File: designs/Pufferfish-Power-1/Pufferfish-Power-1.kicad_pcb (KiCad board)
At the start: 2 copper layers, 138 parts, among them J1 POWER_JACK_PTH, J2 POWER_JACK_PTH, J3 Molex_PicoFlex_20_Vertical, J4 Molex_MicroFit3_2x4_Receptacle, Q1 BSC028N06LS3, Q1 SiR158DP, Q2 BSC028N06LS3, Q2 SiR158DP, Q3 BSC028N06LS3, Q3 SiR158DP, Q4 BSC028N06LS3, Q4 SiR158DP, Q5 2N7002E, Q6 SiSS27DN, Q7 SiSS27DN, Q8 TP0610T, Q9 2N7002E, U1 LTC4421IUHE, U2 TPS568215RNN, U3 TPS82130

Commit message: - Changed polarity of active low LED indicators - Added footprints for test points, inductors and mounting holes - Added ESD protection on interface connectors
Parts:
- added D10: LED_SMD_0603_GREEN, LED_SMD:LED_0603_1608Metric, F.Cu at (174.5, 39.6)
- added D11: LED_SMD_0603_BLUE, LED_SMD:LED_0603_1608Metric, F.Cu at (174.5, 37.0)
- added D12: LED_SMD_0603_BLUE, LED_SMD:LED_0603_1608Metric, F.Cu at (164.5, 44.1)
- added D13: ESDLC5V0PB8, Package_DFN_QFN:UDFN-9_1.0x3.8mm_P0.5mm, F.Cu at (48.3, 61.0)
- added D14: TVS_15V_SOD123FL-2, Diode_SMD:D_SOD-123F, F.Cu at (44.0, 60.0)
- added D15: ESDLC5V0PB8, Package_DFN_QFN:UDFN-9_1.0x3.8mm_P0.5mm, F.Cu at (51.4, 61.0)
- added D3: LED_SMD_0603_YELLOW, LED_SMD:LED_0603_1608Metric, F.Cu at (168.9, 50.8)
- added D4: LED_SMD_0603_YELLOW, LED_SMD:LED_0603_1608Metric, F.Cu at (181.3, 50.8)
- added D5: LED_SMD_0603_ORANGE, LED_SMD:LED_0603_1608Metric, F.Cu at (199.1, 40.8)
- added D6: LED_SMD_0603_ORANGE, LED_SMD:LED_0603_1608Metric, F.Cu at (199.1, 32.5)
- added D7: LED_SMD_0603_RED, LED_SMD:LED_0603_1608Metric, F.Cu at (173.4, 42.2)
- added D8: LED_SMD_0603_RED, LED_SMD:LED_0603_1608Metric, F.Cu at (183.4, 32.5)
- added D9: LED_SMD_0603_GREEN, LED_SMD:LED_0603_1608Metric, F.Cu at (178.5, 37.0)
- added H1: STANDOFF_ELECTRICAL, MountingHole:MountingHole_3.2mm_M3_Pad_Via, F.Cu at (45.2, 43.7)
- added H2: STANDOFF_ELECTRICAL, MountingHole:MountingHole_3mm_Pad_Via, F.Cu at (45.0, 51.5)
- added H3: STANDOFF_ELECTRICAL, MountingHole:MountingHole_3.2mm_M3_Pad_Via, F.Cu at (53.1, 43.7)
- added H4: STANDOFF_ELECTRICAL, MountingHole:MountingHole_3mm_Pad_Via, F.Cu at (52.5, 51.5)
- added H5: STANDOFF_ELECTRICAL, MountingHole:MountingHole_3mm_Pad_Via, F.Cu at (60.9, 43.5)
- added H6: STANDOFF_ELECTRICAL, MountingHole:MountingHole_3mm_Pad_Via, F.Cu at (60.1, 51.5)
- added J5: Molex_MicroFit_2P, Connector_Molex:Molex_Micro-Fit_3.0_43045-0200_2x01_P3.00mm_Horizontal, F.Cu at (76.4, 49.7)
- added J6: Molex_MicroFit_2P, Connector_Molex:Molex_Micro-Fit_3.0_43045-0200_2x01_P3.00mm_Horizontal, F.Cu at (85.7, 49.7)
- added L1: PM2201.122NLT, Pufferfish:L_Pulse_PA5001, F.Cu at (180.3, 87.6)
- added Q10: 2N7002E, Package_TO_SOT_SMD:SOT-23, F.Cu at (164.6, 51.8)
- added Q11: 2N7002E, Package_TO_SOT_SMD:SOT-23, F.Cu at (177.0, 51.8)
- added Q12: 2N7002E, Package_TO_SOT_SMD:SOT-23, F.Cu at (194.8, 41.7)
- added Q13: 2N7002E, Package_TO_SOT_SMD:SOT-23, F.Cu at (194.8, 33.5)
- added Q14: TP0610T, Package_TO_SOT_SMD:SOT-23, F.Cu at (93.7, 68.9)
- added Q14: 2N7002E, Package_TO_SOT_SMD:SOT-23, F.Cu at (164.6, 40.6)
- added Q15: TP0610T, Package_TO_SOT_SMD:SOT-23, F.Cu at (89.2, 68.9)
- added Q15: 2N7002E, Package_TO_SOT_SMD:SOT-23, F.Cu at (170.2, 38.0)
- added Q16: TP0610T, Package_TO_SOT_SMD:SOT-23, F.Cu at (89.2, 59.8)
- added Q16: 2N7002E, Package_TO_SOT_SMD:SOT-23, F.Cu at (169.1, 42.6)
- added Q17: TP0610T, Package_TO_SOT_SMD:SOT-23, F.Cu at (93.7, 64.4)
- added Q17: 2N7002E, Package_TO_SOT_SMD:SOT-23, F.Cu at (174.6, 33.5)
- added Q18: TP0610T, Package_TO_SOT_SMD:SOT-23, F.Cu at (89.2, 64.4)
- added Q18: 2N7002E, Package_TO_SOT_SMD:SOT-23, F.Cu at (170.2, 33.5)
- added Q19: TP0610T, Package_TO_SOT_SMD:SOT-23, F.Cu at (93.7, 59.8)
- added Q19: 2N7002E, Package_TO_SOT_SMD:SOT-23, F.Cu at (179.1, 33.5)
- added R24: RES_330R_0603_SMD, Pufferfish:RES_SMD_0603, F.Cu at (168.9, 53.4)
- added R25: RES_330R_0603_SMD, Pufferfish:RES_SMD_0603, F.Cu at (181.2, 53.4)
- added R53: RES_330R_0603_SMD, Pufferfish:RES_SMD_0603, F.Cu at (199.1, 43.3)
- added R54: RES_330R_0603_SMD, Pufferfish:RES_SMD_0603, F.Cu at (199.1, 35.0)
- added R55: RES_330R_0603_SMD, Pufferfish:RES_SMD_0603, F.Cu at (177.4, 42.2)
- added R56: RES_330R_0603_SMD, Pufferfish:RES_SMD_0603, F.Cu at (182.5, 39.6)
- added R57: RES_330R_0603_SMD, Pufferfish:RES_SMD_0603, F.Cu at (187.4, 32.5)
- added R58: RES_330R_0603_SMD, Pufferfish:RES_SMD_0603, F.Cu at (178.5, 39.6)
- added R59: RES_330R_0603_SMD, Pufferfish:RES_SMD_0603, F.Cu at (182.5, 37.0)
- added R60: RES_330R_0603_SMD, Pufferfish:RES_SMD_0603, F.Cu at (173.3, 44.8)
- added TP1: TP_TH_KEYSTONE_5010, TestPoint:TestPoint_Keystone_5010-5014_Multipurpose, F.Cu at (59.5, 60.8)
- added TP10: TP_TH_KEYSTONE_5126, TestPoint:TestPoint_Keystone_5010-5014_Multipurpose, F.Cu at (79.4, 60.1)
- added TP11: TP_TH_KEYSTONE_5126, TestPoint:TestPoint_Keystone_5010-5014_Multipurpose, F.Cu at (74.4, 65.1)
- added TP12: TP_TH_KEYSTONE_5126, TestPoint:TestPoint_Keystone_5010-5014_Multipurpose, F.Cu at (74.4, 60.1)
- added TP13: TP_TH_KEYSTONE_5126, TestPoint:TestPoint_Keystone_5010-5014_Multipurpose, F.Cu at (84.5, 60.1)
- added TP14: TP_TH_KEYSTONE_5126, TestPoint:TestPoint_Keystone_5010-5014_Multipurpose, F.Cu at (84.5, 65.1)
- added TP2: TP_TH_KEYSTONE_5010, TestPoint:TestPoint_Keystone_5010-5014_Multipurpose, F.Cu at (92.8, 42.3)
- added TP3: TP_TH_KEYSTONE_5010, TestPoint:TestPoint_Keystone_5010-5014_Multipurpose, F.Cu at (92.8, 47.3)
- added TP4: TP_TH_KEYSTONE_5126, TestPoint:TestPoint_Keystone_5010-5014_Multipurpose, F.Cu at (237.0, 56.3)
- added TP5: TP_TH_KEYSTONE_5010, TestPoint:TestPoint_Keystone_5010-5014_Multipurpose, F.Cu at (249.9, 47.7)
- added TP6: TP_TH_KEYSTONE_5010, TestPoint:TestPoint_Keystone_5010-5014_Multipurpose, F.Cu at (237.0, 47.7)
- added TP7: TP_SMT_KEYSTONE_5019, Pufferfish:TP380X203, F.Cu at (165.2, 36.5)
- added TP8: TP_SMT_KEYSTONE_5019, Pufferfish:TP380X203, F.Cu at (165.2, 33.0)
- added TP9: TP_TH_KEYSTONE_5126, TestPoint:TestPoint_Keystone_5010-5014_Multipurpose, F.Cu at (79.4, 65.1)
- moved C1 25.4 mm to (115.6, 156.2)
- moved C10 25.4 mm to (183.1, 133.3)
- moved C11 25.4 mm to (187.7, 129.1)
- moved C12 25.4 mm to (161.4, 126.4)
- moved C13 25.4 mm to (176.1, 126.4)
- moved C14 25.4 mm to (96.5, 116.8)
- moved C15 25.4 mm to (92.1, 116.8)
- moved C16 25.4 mm to (91.4, 119.3)
- moved C17 25.4 mm to (113.2, 108.4)
- moved C18 25.4 mm to (110.3, 108.4)
- moved C19 25.4 mm to (111.9, 105.9)
- moved C2 25.4 mm to (115.6, 158.7)
- moved C20 25.4 mm to (107.5, 105.9)
- moved C21 25.4 mm to (103.1, 105.9)
- moved C22 25.4 mm to (96.6, 109.2)
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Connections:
- net /Interface and LEDs/BAT-MEAS-ANALOG renamed /Interface/BAT-MEAS-ANALOG
- net /Interface and LEDs/BAT-MEAS-EN renamed /Interface/BAT-MEAS-EN

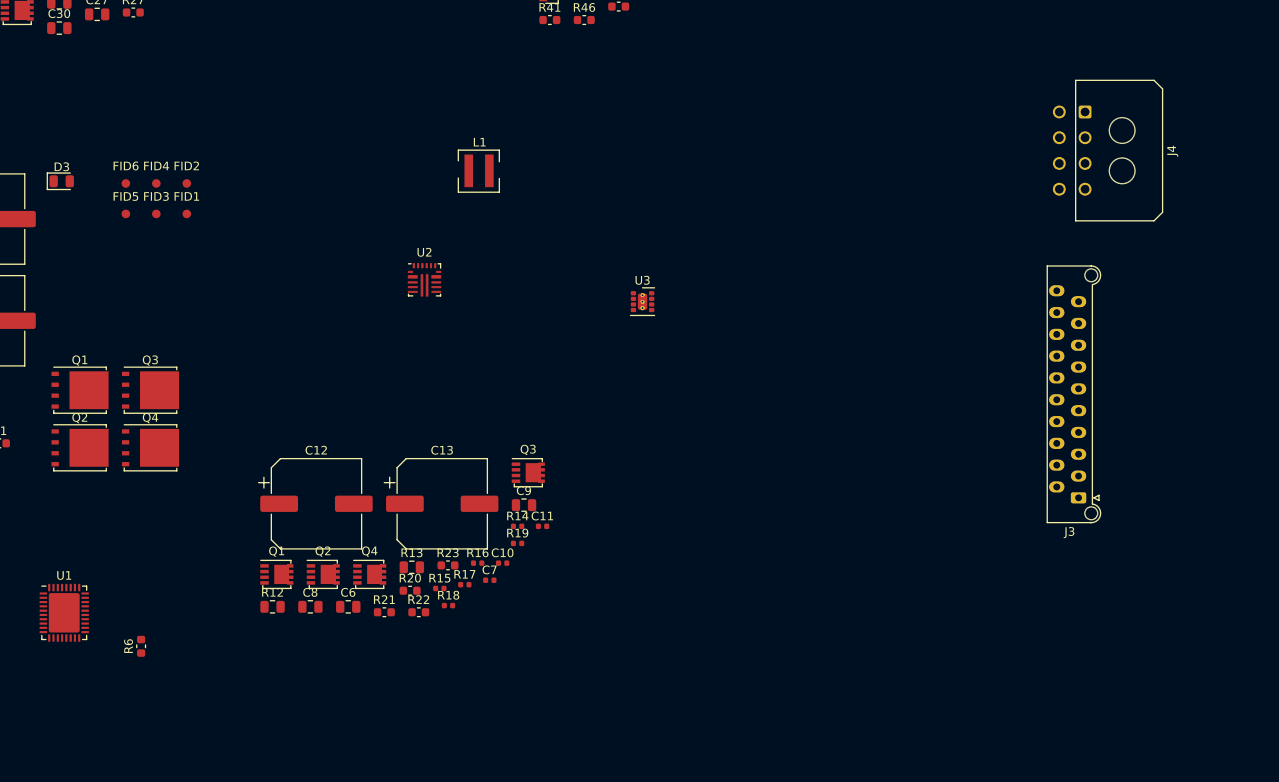
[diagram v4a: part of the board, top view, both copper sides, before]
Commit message: - Fixed layout footprint - Changed title of LTC4421 sheet
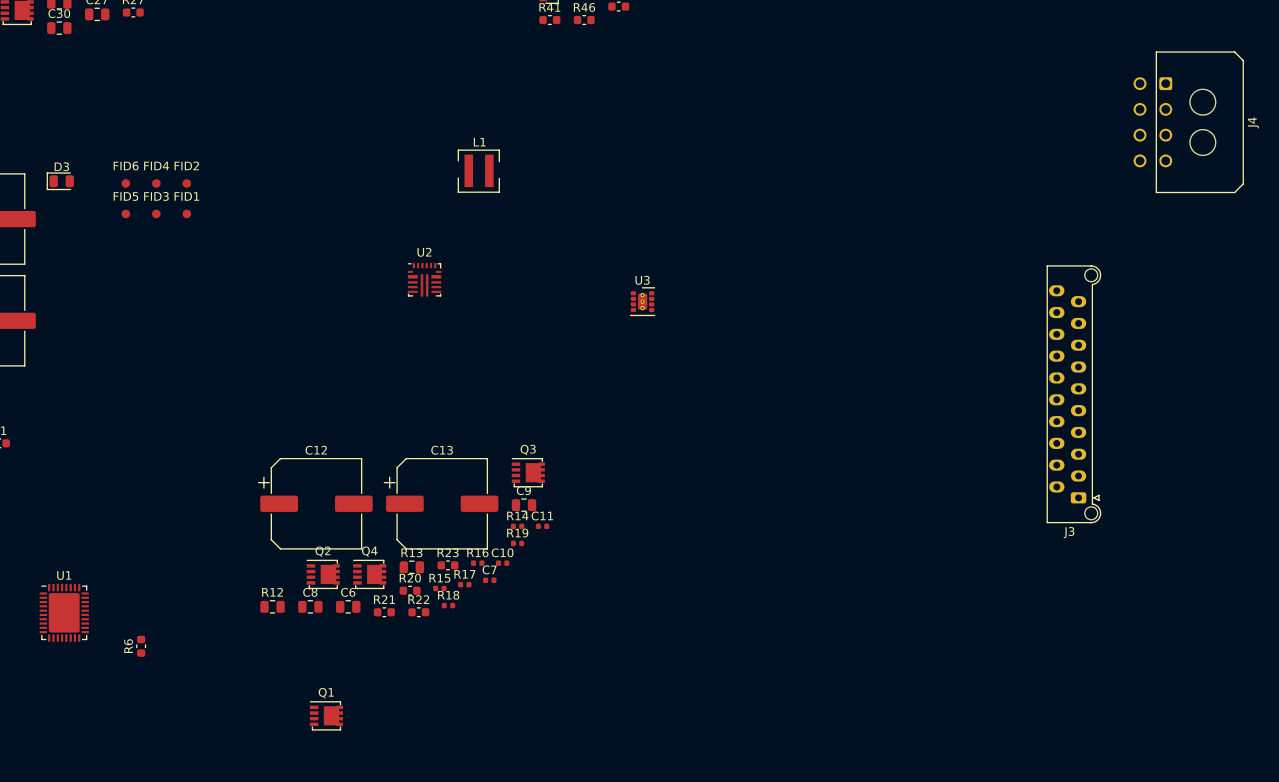
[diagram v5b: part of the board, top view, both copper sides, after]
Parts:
- removed the Q1 at (133.8, 113.2)
- removed the Q2 at (133.8, 119.9)
- removed the Q3 at (142.1, 113.2)
- removed the Q4 at (142.1, 119.9)
- moved Q1 17.5 mm to (162.6, 151.1)
- moved J4 9.96 mm to (260.4, 77.5)
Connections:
- H1 pad 1: (no net) -> GND
- H2 pad 1: (no net) -> GND
- H3 pad 1: (no net) -> GND
- H4 pad 1: (no net) -> GND
- H5 pad 1: (no net) -> GND
- H6 pad 1: (no net) -> GND
- Q1 pad 5: Net-(Q1-Pad5) -> VIN-PRIMARY-12V0
- Q2 pad 5: Net-(Q2-Pad5) -> /LTC4221/LTC4421-SENSE
- Q3 pad 5: Net-(Q3-Pad5) -> VIN-BACKUP-12V0
- Q4 pad 5: Net-(Q4-Pad5) -> /LTC4221/LTC4421-SENSE
